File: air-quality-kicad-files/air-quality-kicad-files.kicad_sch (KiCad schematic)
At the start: 10 parts, among them U2 XIAO-ESP32C3

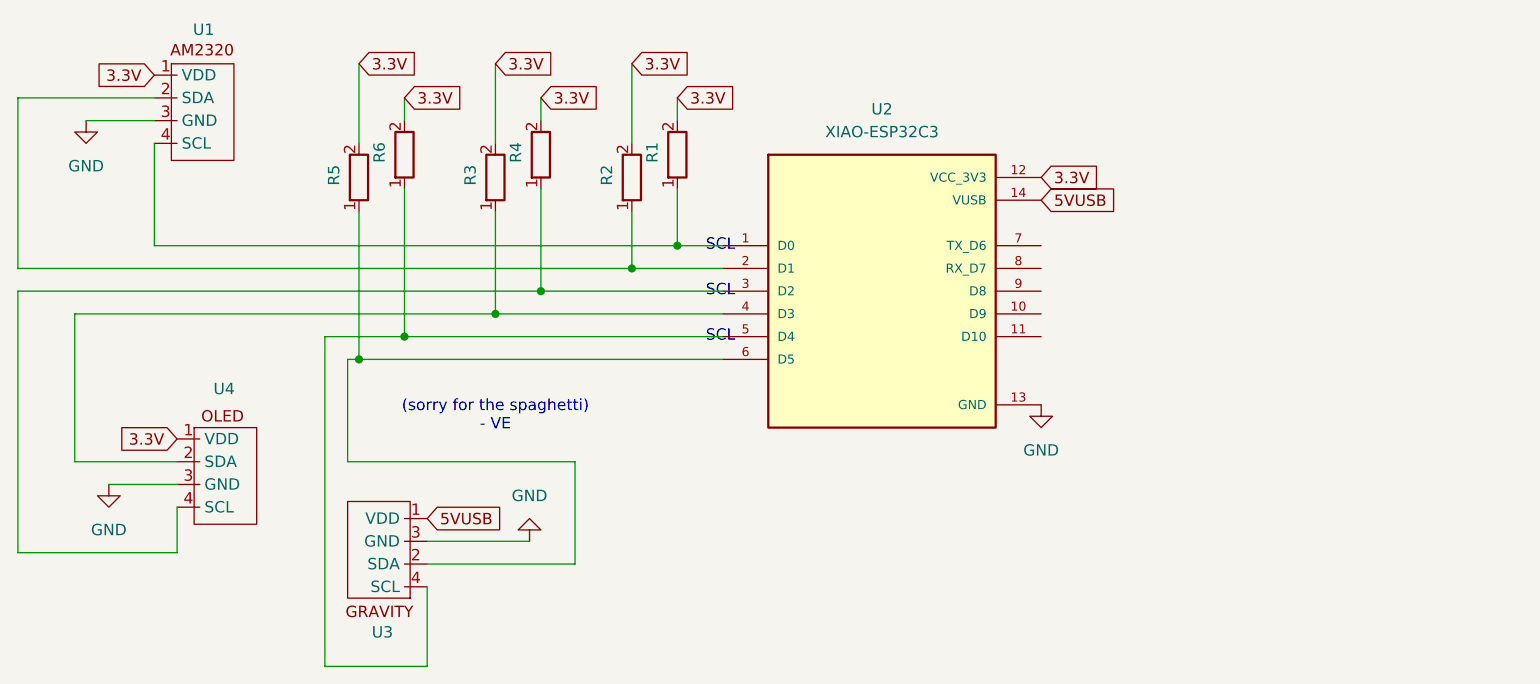
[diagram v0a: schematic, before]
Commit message: added resistors, buzzer circuit, holes, cleaned up files
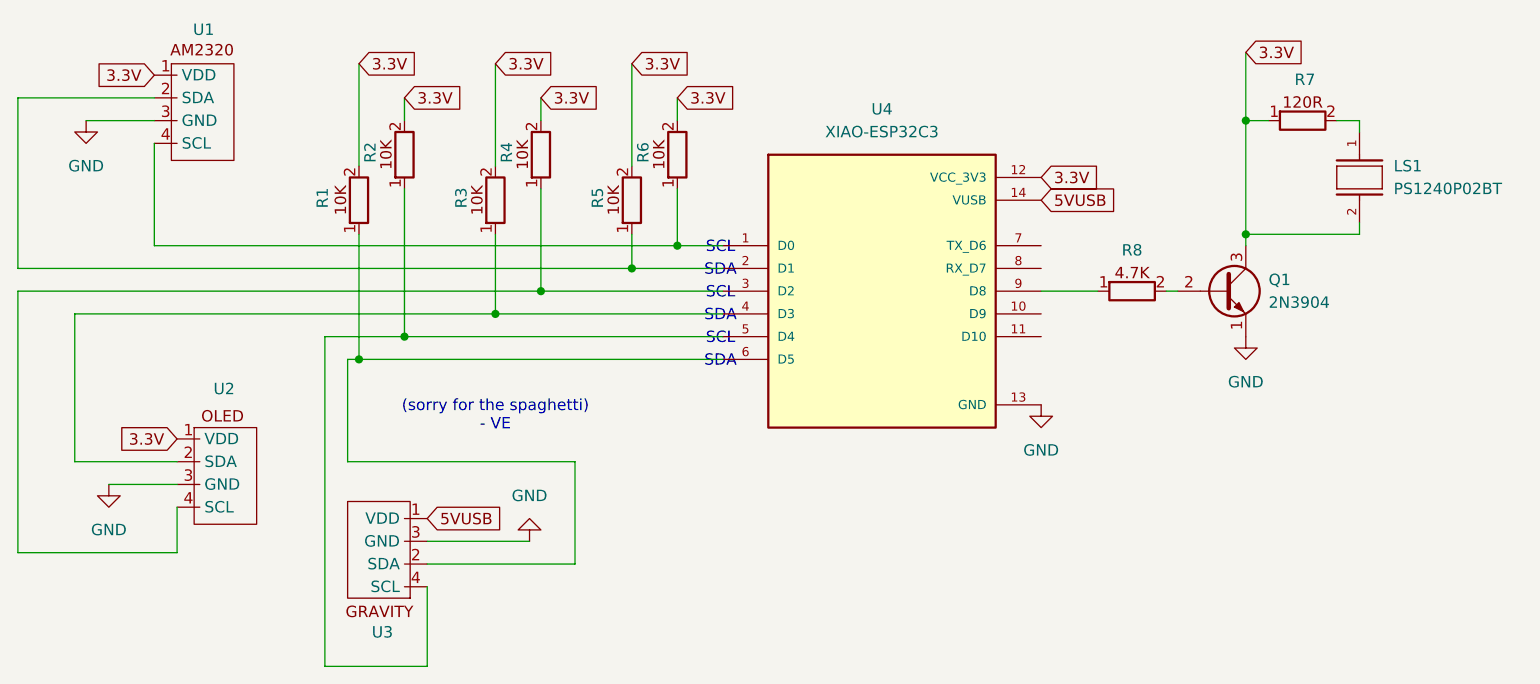
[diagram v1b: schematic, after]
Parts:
- added LS1: PS1240P02BT, footprints:buzzer-XDCR_PS1240P02BT, symbol custom-symbols:PS1240P02BT
- added Q1: 2N3904, Package_TO_SOT_THT:TO-92_Inline, symbol Transistor_BJT:2N3904
- added R7: ~, footprints:120R, symbol custom-symbols:120R
- added R8: ~, footprints:4-7K, symbol custom-symbols:4-7K
- renumbered R5 to R1, R6 to R2, R2 to R5, R1 to R6, U4 to U2, U2 to U4
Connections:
- net 3.3V: now also LS1.2, Q1.3 (C), R7.1
- net GND: now also Q1.1 (E)
- net at U4.9 (D8): now also R8.1
- new net: Q1.2 (B), R8.2
- new net: LS1.1, R7.2
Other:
- note added: "SDA"
